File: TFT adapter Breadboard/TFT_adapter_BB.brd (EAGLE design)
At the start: 26.6 x 20 mm, 3 parts

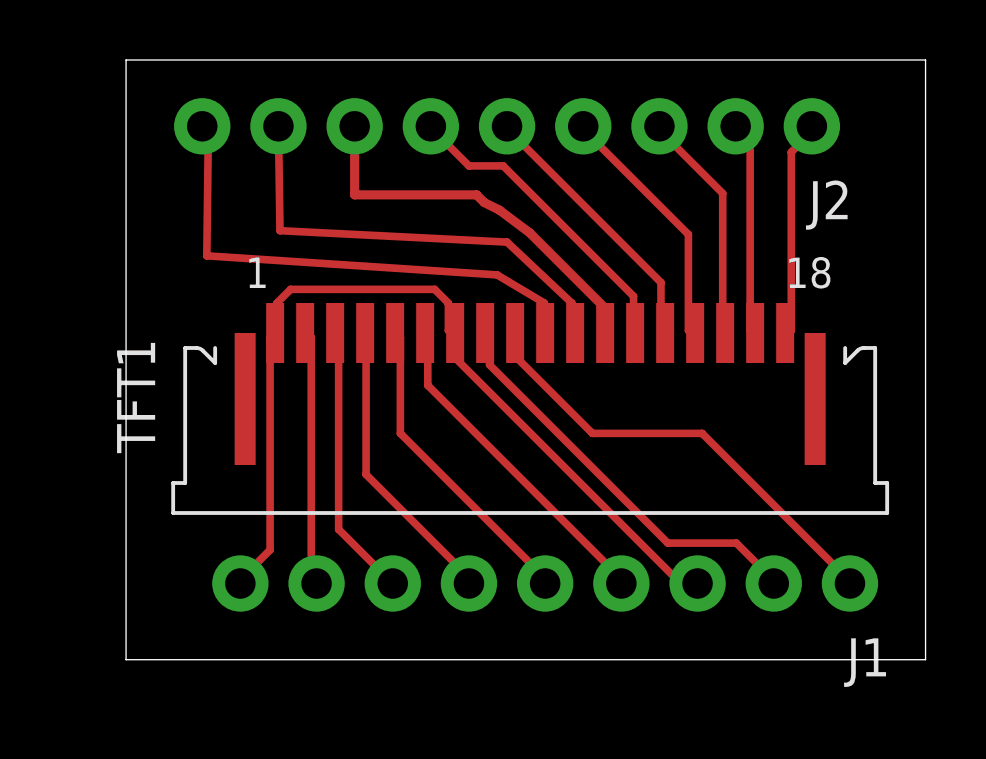
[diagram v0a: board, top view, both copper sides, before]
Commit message: Added the breadboard TFT adapater
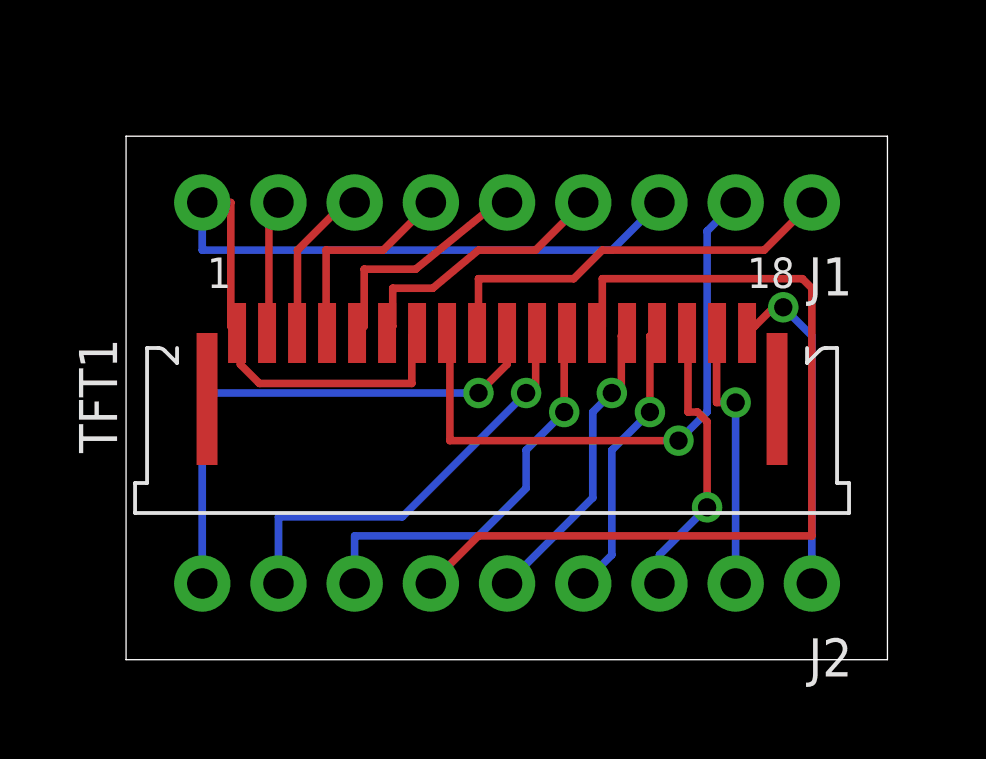
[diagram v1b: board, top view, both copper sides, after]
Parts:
- moved J2 15.2 mm to (22.9, 2.54)
- moved J1 12.8 mm to (22.9, 15.2)
- moved TFT1 1.27 mm to (12.7, 8.89)
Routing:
- net N$16: track 10.4 -> 30.6 mm
- net GND2: track 13.7 -> 20.0 mm, vias 0 -> 1
- net N$10: track 7.31 -> 11.2 mm, vias 0 -> 1
- net N$2: track 8.52 -> 4.68 mm
- net N$3: track 9.14 -> 5.33 mm
- net N$4: track 9.77 -> 6.91 mm
- net N$5: track 10.4 -> 7.78 mm
- net GND: track 29.2 -> 31.7 mm
- net N$6: track 11.0 -> 9.03 mm
- net N$11: track 7.19 -> 8.99 mm, vias 0 -> 1
- net N$12: track 7.78 -> 9.46 mm, vias 0 -> 1
- net N$14: track 9.08 -> 10.2 mm, vias 0 -> 1
- net VDD: track 15.1 -> 14.0 mm
- net LEDA: track 16.9 -> 18.0 mm, vias 0 -> 1
- net N$13: track 8.48 -> 9.43 mm, vias 0 -> 1
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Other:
- board size 26.6 x 20 mm -> 25.4 x 17.4 mm
